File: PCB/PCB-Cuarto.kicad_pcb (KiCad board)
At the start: 2 copper layers, 90 x 100 mm, 80 parts, among them IC100 AP63203WU-7, J100 2604-3102, J2 2086-1104, J200 TYPE-C-31-M-12, J300 2086-1102, J301 jumper, J302 2086-1104, J303 2086-1104, Q100 CSD19537Q3, Q101 BSS138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

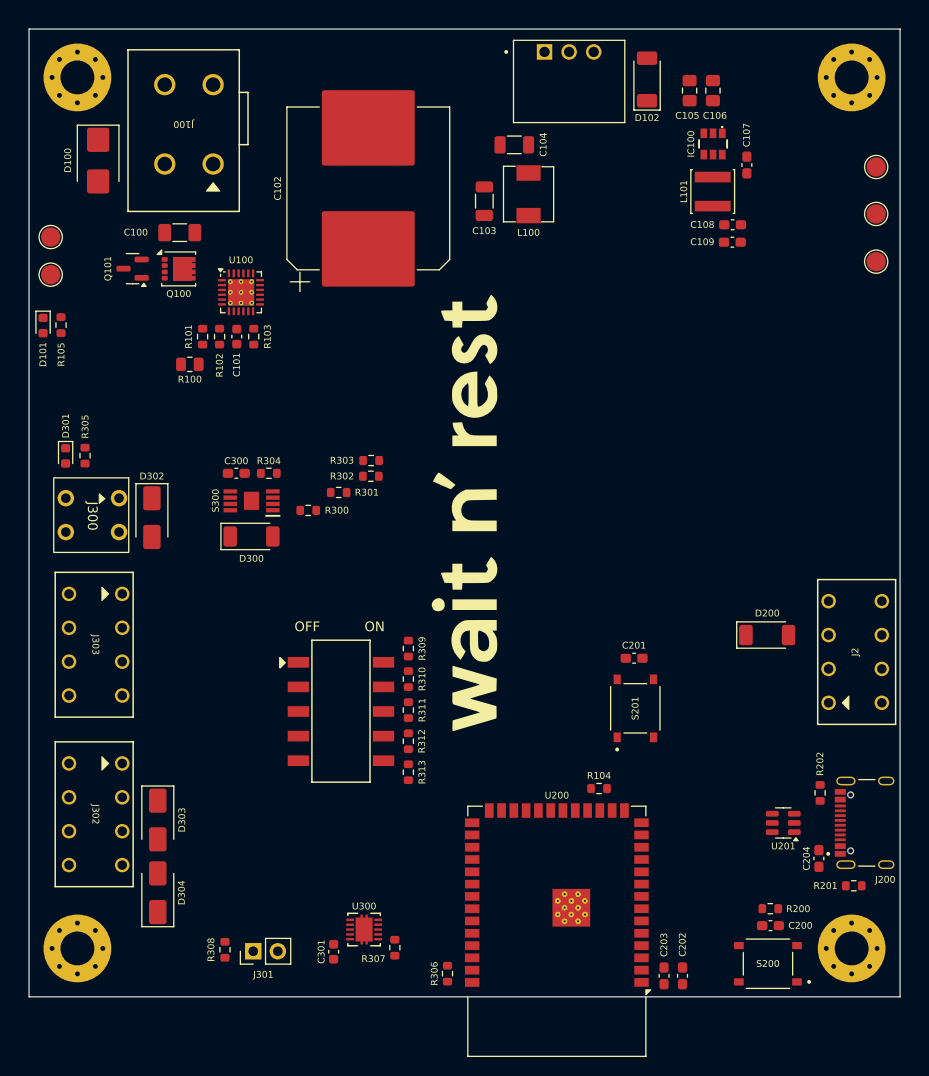
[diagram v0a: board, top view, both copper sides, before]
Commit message: PCB acabada con labels
Se agrego:
- Planos de tierra
- Stitching vias
- Labels indicadores para todo los conectores

Se corrigio:
- Errores de librerias de footprint - TPS26631RGE
- Pines sin conectarse
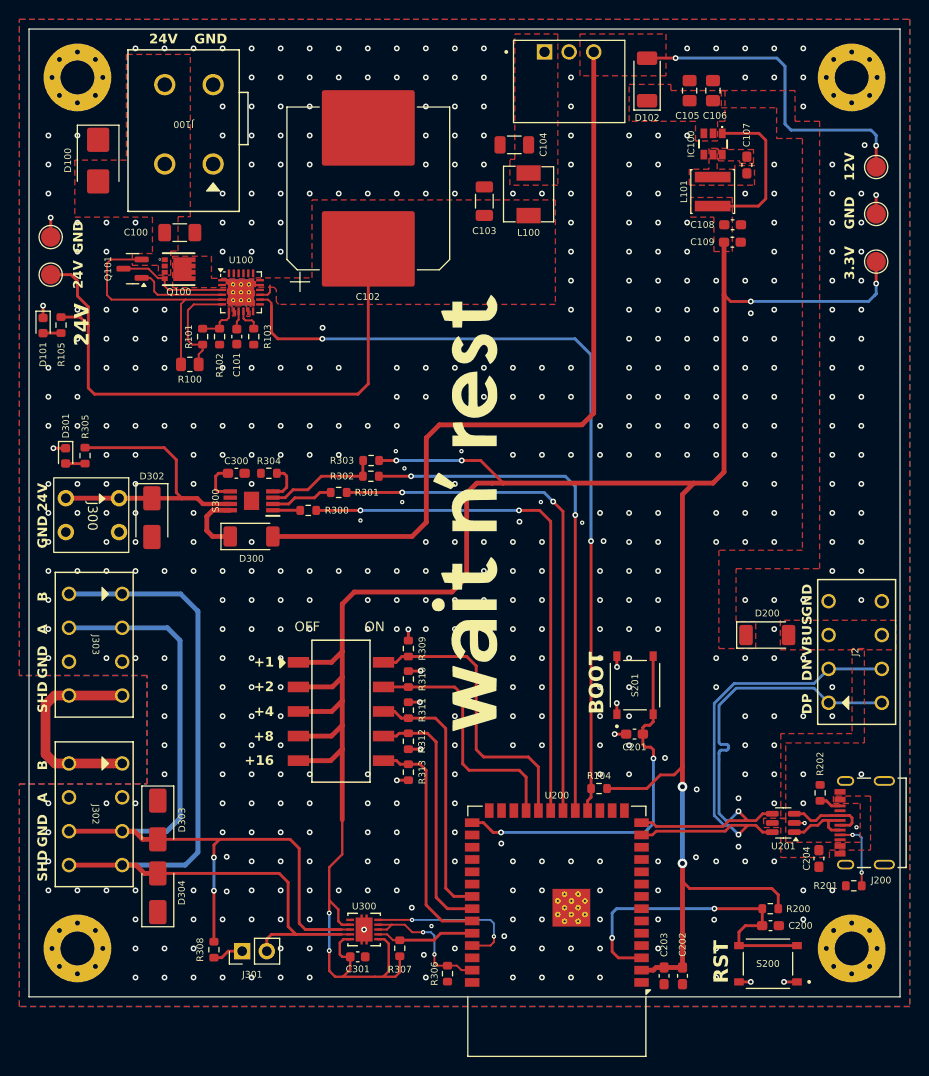
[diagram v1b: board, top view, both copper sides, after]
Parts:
- J200: value TYPE-C-31-M-12 -> 2171790001; footprint TYPE-C-31-M-12:TYPE-C-31-M-12 -> 2171790001:MOLEX_2171790001
- Q100: footprint Package_SON:VSON-8_3.3x3.3mm_P0.65mm_NexFET -> CSD19537Q3:CSD19537Q3
- moved C201 7.84 mm to (167.6, 120.9)
- moved C301 2.54 mm to (139.0, 143.9), turned to 0 degrees
- moved S201 2.39 mm to (167.6, 115.8)
- moved J200 1.35 mm to (192.2, 130.0)
- moved R308 1.14 mm to (124.1, 143.1)
- moved J301 1.14 mm to (127.0, 143.3)
- moved R307 0.51 mm to (143.3, 143.0)
- turned Q100 to -90 degrees
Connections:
- Q100 pad 2: /POWER/INPUT -> Net-(Q100-G)
- Q100 pad 3: /POWER/INPUT -> Net-(Q100-D)
- U201 pad 4: /MCU/USB_N -> /MCU/USB_P
- U201 pad 6: /MCU/USB_P -> /MCU/USB_N
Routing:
- net +3.3V: track 0.00 -> 287.2 mm, vias 0 -> 8
- net +12V: track 0.00 -> 114.6 mm, vias 0 -> 2
- net /PERIPHERALS/B: track 0.00 -> 86.5 mm
- net /MCU/FLT: track 0.00 -> 85.6 mm, vias 0 -> 2
- net /PERIPHERALS/A: track 0.00 -> 85.5 mm, vias 0 -> 2
- net +24V: track 0.00 -> 63.1 mm
- net /MCU/DOOR_EN: track 0.00 -> 54.6 mm, vias 0 -> 2
- net /MCU/DOOR_FAULT: track 0.00 -> 54.2 mm, vias 0 -> 2
- net /MCU/DOOR_DIAG_EN: track 0.00 -> 54.1 mm, vias 0 -> 2
- net /MCU/USB_N: track 0.00 -> 49.3 mm, vias 0 -> 1
- net /MCU/USB_P: track 0.00 -> 49.2 mm, vias 0 -> 1
- net /MCU/BOOT: track 0.00 -> 38.3 mm, vias 0 -> 2
- net /MCU/EN: track 0.00 -> 34.8 mm, vias 0 -> 2
- net Net-(D302-A1): track 0.00 -> 31.4 mm
- net /ID1: track 0.00 -> 30.5 mm
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- added copper zone on F.Cu, net +12V
- added copper zone on F.Cu, net +24V
- added copper zone on F.Cu, net +3.3V
- added copper zone on F.Cu, net /12V_5V
- added copper zone on F.Cu, net /POWER/INPUT
- added copper zone on B.Cu, net GND
- added copper zone on F.Cu, net GND
- added copper zone on In1.Cu, net GND
- added copper zone on In2.Cu, net GND
- added copper zone on F.Cu, net Net-(IC100-BST)
- added copper zone on F.Cu, net Net-(IC100-SW)
- added copper zone on F.Cu, net Net-(PS100-+VIN)
- added copper zone on F.Cu, net Net-(Q100-D)
- added copper zone on F.Cu, net VBUS
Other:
- copper layers 2 -> 4
- board text added: "+1"
- board text added: "+16"
- board text added: "+2"
- board text added: "+4"
- board text added: "+8"
- board text added: "12V"
- board text added: "24V"
- board text added: "3.3V"
- board text added: "A"
- board text added: "B"
- board text added: "BOOT"
- board text added: "DN"
- board text added: "DP"
- board text added: "GND"
- board text added: "RST"
- board text added: "SHD"
- board text added: "VBUS"

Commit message: Edicion de archivos para JLCPCB
Se ha realizado:
- Cambio de footprint de capacitor 1mF
- Edicion de algunos value references
- Creación de archivos para JLCPCB
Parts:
- C102: footprint Capacitor_SMD:CP_Elec_16x17.5 -> VKMI1701H102MV:VKMI1701H102MV
- renumbered J2 to J201
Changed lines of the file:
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@@
 		(at 187.616201 117.617001 90)
 		(tags "2086-1104 ")
-		(property "Reference" "J2"
+		(property "Reference" "J201"
 			(at 5.25 2.75 90)
 			(unlocked yes)
@@
 		)
 	)
-	(footprint "Capacitor_SMD:CP_Elec_16x17.5"
+	(footprint "VKMI1701H102MV:VKMI1701H102MV"
 		(layer "F.Cu")
 		(at 140.0556 64.4668 90)
-		(descr "SMD capacitor, aluminum electrolytic, Vishay 1616, 16.0x17.5mm, http://www.vishay.com/docs/28395/150crz.pdf")
-		(tags "capacitor electrolytic")
 		(property "Reference" "C102"
-			(at -11.1998 -0.0508 180)
+			(at 0 -0.5 90)
+			(unlocked yes)
 			(layer "F.SilkS")
 			(effects
 				(font
-					(size 0.7 0.7)
-					(thickness 0.15)
+					(size 1 1)
+					(thickness 0.1)
 				)
 			)
 		)
 		(property "Value" "1mF/50V"
-			(at 0 9.35 90)
+			(at 0 1 90)
+			(unlocked yes)
 			(layer "F.Fab")
 			(effects
@@
 			)
 		)
-		(property "Footprint" "Capacitor_SMD:CP_Elec_16x17.5"
+		(property "Footprint" "VKMI1701H102MV:VKMI1701H102MV"
 			(at 0 0 90)
 			(unlocked yes)
@@
 			(effects
 				(font
-					(size 1.27 1.27)
+					(size 1 1)
 					(thickness 0.15)
 				)
@@
 			(effects
 				(font
-					(size 1.27 1.27)
+					(size 1 1)
 					(thickness 0.15)
 				)
@@
 			(effects
 				(font
-					(size 1.27 1.27)
+					(size 1 1)
 					(thickness 0.15)
 				)
@@
 		(attr smd)
 		(fp_line
-			(start 8.41 -8.41)
-			(end 8.41 -5.06)
+			(start 8.5976 -8.2224)
+			(end 8.5976 -4.8724)
 			(stroke
 				(width 0.12)
@@
 		)
 		(fp_line
-			(start -7.345563 -8.41)
-			(end 8.41 -8.41)
+			(start -7.157963 -8.2224)
+			(end 8.5976 -8.2224)
 			(stroke
 				(width 0.12)
@@
 		)
 		(fp_line
-			(start -9.65 -8.06)
-			(end -9.65 -6.06)
+			(start -9.4624 -7.8724)
+			(end -9.4624 -5.8724)
 			(stroke
 				(width 0.12)
@@
 		)
 		(fp_line
-			(start -8.41 -7.345563)
-			(end -7.345563 -8.41)
+			(start -8.2224 -7.157963)
+			(end -7.157963 -8.2224)
 			(stroke
 				(width 0.12)
@@
 		)
 		(fp_line
-			(start -8.41 -7.345563)
-			(end -8.41 -5.06)
+			(start -8.2224 -7.157963)
+			(end -8.2224 -4.8724)
 			(stroke
 				(width 0.12)
@@
 		)
 		(fp_line
-			(start -10.65 -7.06)
-			(end -8.65 -7.06)
+			(start -10.4624 -6.8724)
+			(end -8.4624 -6.8724)
 			(stroke
 				(width 0.12)
@@
 		)
 		(fp_line
-			(start -8.41 7.345563)
-			(end -8.41 5.06)
+			(start -8.2224 7.533163)
+			(end -8.2224 5.2476)
 			(stroke
 				(width 0.12)
@@
 		)
 		(fp_line
-			(start -8.41 7.345563)
-			(end -7.345563 8.41)
+			(start -8.2224 7.533163)
+			(end -7.157963 8.5976)
 			(stroke
 				(width 0.12)
@@
 		)
 		(fp_line
-			(start 8.41 8.41)
-			(end 8.41 5.06)
+			(start 8.5976 8.5976)
+			(end 8.5976 5.2476)
 			(stroke
 				(width 0.12)
@@
 		)
 		(fp_line
-			(start -7.345563 8.41)
-			(end 8.41 8.41)
+			(start -7.157963 8.5976)
+			(end 8.5976 8.5976)
 			(stroke
 				(width 0.12)
@@
 		)
 		(fp_line
-			(start 8.55 -8.55)
-			(end 8.55 -5.05)
+			(start 8.7376 -8.3624)
+			(end 8.7376 -4.8624)
 			(stroke
 				(width 0.05)
@@
 		)
 		(fp_line
-			(start -7.4 -8.55)
-			(end 8.55 -8.55)
+			(start -7.2124 -8.3624)
+			(end 8.7376 -8.3624)
 			(stroke
 				(width 0.05)
@@
 		)
 		(fp_line
-			(start -8.55 -7.4)
-			(end -7.4 -8.55)
+			(start -8.3624 -7.2124)
+			(end -7.2124 -8.3624)
 			(stroke
 				(width 0.05)
@@
 		)
 		(fp_line
-			(start -8.55 -7.4)
-			(end -8.55 -5.05)
+			(start -8.3624 -7.2124)
+			(end -8.3624 -4.8624)
 			(stroke
 				(width 0.05)
@@
 		)
 		(fp_line
-			(start 10.4 -5.05)
-			(end 10.4 5.05)
+			(start 10.5876 -4.8624)
+			(end 10.5876 5.2376)
 			(stroke
 				(width 0.05)
@@
 		)
 		(fp_line
-			(start 8.55 -5.05)
-			(end 10.4 -5.05)
+			(start 8.7376 -4.8624)
+			(end 10.5876 -4.8624)
 			(stroke
 				(width 0.05)
@@
 		)
 		(fp_line
-			(start -8.55 -5.05)
-			(end -10.4 -5.05)
+			(start -8.3624 -4.8624)
+			(end -10.2124 -4.8624)
 			(stroke
 				(width 0.05)
@@
 		)
 		(fp_line
-			(start -10.4 -5.05)
-			(end -10.4 5.05)
+			(start -10.2124 -4.8624)
+			(end -10.2124 5.2376)
 			(stroke
 				(width 0.05)
@@
 		)
 		(fp_line
-			(start 10.4 5.05)
-			(end 8.55 5.05)
+			(start 10.5876 5.2376)
+			(end 8.7376 5.2376)
 			(stroke
 				(width 0.05)
@@
 		)
 		(fp_line
-			(start 8.55 5.05)
-			(end 8.55 8.55)
+			(start 8.7376 5.2376)
+			(end 8.7376 8.7376)
 			(stroke
 				(width 0.05)
@@
 		)
 		(fp_line
-			(start -8.55 5.05)
-			(end -8.55 7.4)
+			(start -8.3624 5.2376)
+			(end -8.3624 7.5876)
 			(stroke
 				(width 0.05)
@@
 		)
 		(fp_line
-			(start -10.4 5.05)
-			(end -8.55 5.05)
+			(start -10.2124 5.2376)
+			(end -8.3624 5.2376)
 			(stroke
 				(width 0.05)
@@
 		)
 		(fp_line
-			(start -8.55 7.4)
-			(end -7.4 8.55)
+			(start -8.3624 7.5876)
+			(end -7.2124 8.7376)
 			(stroke
 				(width 0.05)
@@
 		)
 		(fp_line
-			(start -7.4 8.55)
-			(end 8.55 8.55)
+			(start -7.2124 8.7376)
+			(end 8.7376 8.7376)
 			(stroke
 				(width 0.05)
@@
 		)
 		(fp_line
-			(start 8.3 -8.3)
-			(end 8.3 8.3)
+			(start 8.4876 -8.1124)
+			(end 8.4876 8.4876)
 			(stroke
 				(width 0.1)
@@
 		)
 		(fp_line
-			(start -7.3 -8.3)
-			(end 8.3 -8.3)
+			(start -7.1124 -8.1124)
+			(end 8.4876 -8.1124)
 			(stroke
 				(width 0.1)
@@
 		)
 		(fp_line
-			(start -8.3 -7.3)
-			(end -7.3 -8.3)
+			(start -8.1124 -7.1124)
+			(end -7.1124 -8.1124)
 			(stroke
 				(width 0.1)
@@
 		)
 		(fp_line
-			(start -8.3 -7.3)
-			(end -8.3 7.3)
+			(start -8.1124 -7.1124)
+			(end -8.1124 7.4876)
 			(stroke
 				(width 0.1)
@@
 		)
 		(fp_line
-			(start -6.717142 -3.1)
-			(end -6.717142 -1.5)
+			(start -6.529542 -2.9124)
+			(end -6.529542 -1.3124)
 			(stroke
 				(width 0.1)
@@
 		)
 		(fp_line
-			(start -7.517142 -2.3)
-			(end -5.917142 -2.3)
+			(start -7.329542 -2.1124)
+			(end -5.729542 -2.1124)
 			(stroke
 				(width 0.1)
@@
 		)
 		(fp_line
-			(start -8.3 7.3)
-			(end -7.3 8.3)
+			(start -8.1124 7.4876)
+			(end -7.1124 8.4876)
 			(stroke
 				(width 0.1)
@@
 		)
 		(fp_line
-			(start -7.3 8.3)
-			(end 8.3 8.3)
+			(start -7.1124 8.4876)
+			(end 8.4876 8.4876)
 			(stroke
 				(width 0.1)
@@
 		)
 		(fp_circle
-			(center 0 0)
-			(end 8 0)
+			(center 0.1876 0.1876)
+			(end 8.1876 0.1876)
 			(stroke
 				(width 0.1)
@@
 		)
 		(fp_text user "${REFERENCE}"
-			(at 0 0 90)
+			(at 0.1876 0.1876 90)
+			(layer "F.Fab")
+			(effects
+				(font
+					(size 1 1)
+					(thickness 0.15)
+				)
+			)
+		)
+		(fp_text user "${REFERENCE}"
+			(at 0 2.5 90)
+			(unlocked yes)
 			(layer "F.Fab")
 			(effects
@@
 		)
 		(pad "1" smd roundrect
-			(at -6.25 0 90)
-			(size 7.8 9.6)
+			(at -6.0624 0.1876 90)
+			(size 8 2.5)
 			(layers "F.Cu" "F.Paste" "F.Mask")
 			(roundrect_rratio 0.032051)
@@
 		)
 		(pad "2" smd roundrect
-			(at 6.25 0 90)
-			(size 7.8 9.6)
+			(at 6.4376 0.1876 90)
+			(size 8 2.5)
 			(layers "F.Cu" "F.Paste" "F.Mask")
 			(roundrect_rratio 0.032051)
@@
 			)
 		)
-		(property "LCSC" "C7420339"
+		(property "LCSC" "C40912"
 			(at 0 0 180)
 			(unlocked yes)
